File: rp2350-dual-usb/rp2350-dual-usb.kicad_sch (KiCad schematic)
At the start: 36 parts, among them J1 Conn_01x03_MountingPin, SW1 Button_Switch_SMD_Push_1P1T_W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, U1 LDL1117-3.3, U2 RP2354_60QFN, Y1 12MHz

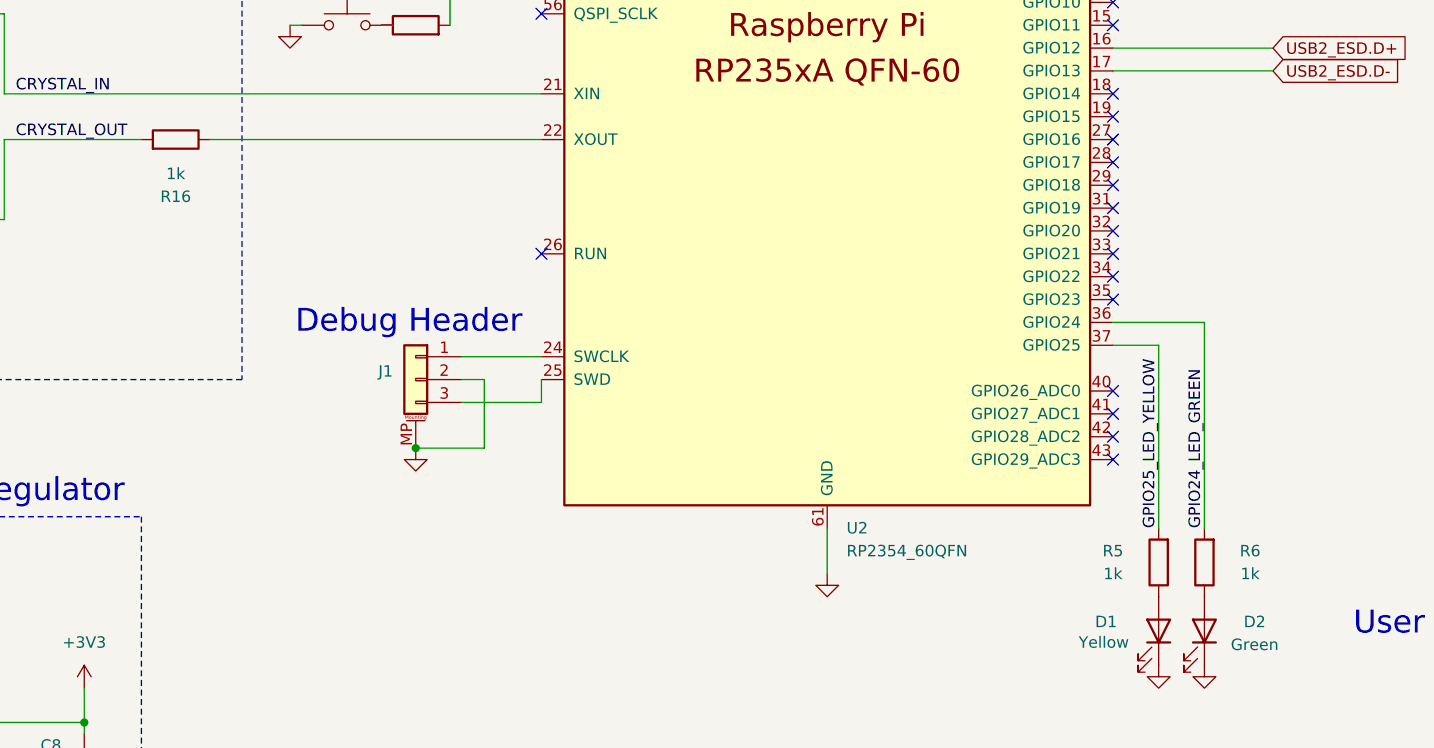
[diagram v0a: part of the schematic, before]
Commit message: Updates YouMe Transformer to v1.1, fixing incorrect R10 value. Improves the consistency of the Lichen symbol library.
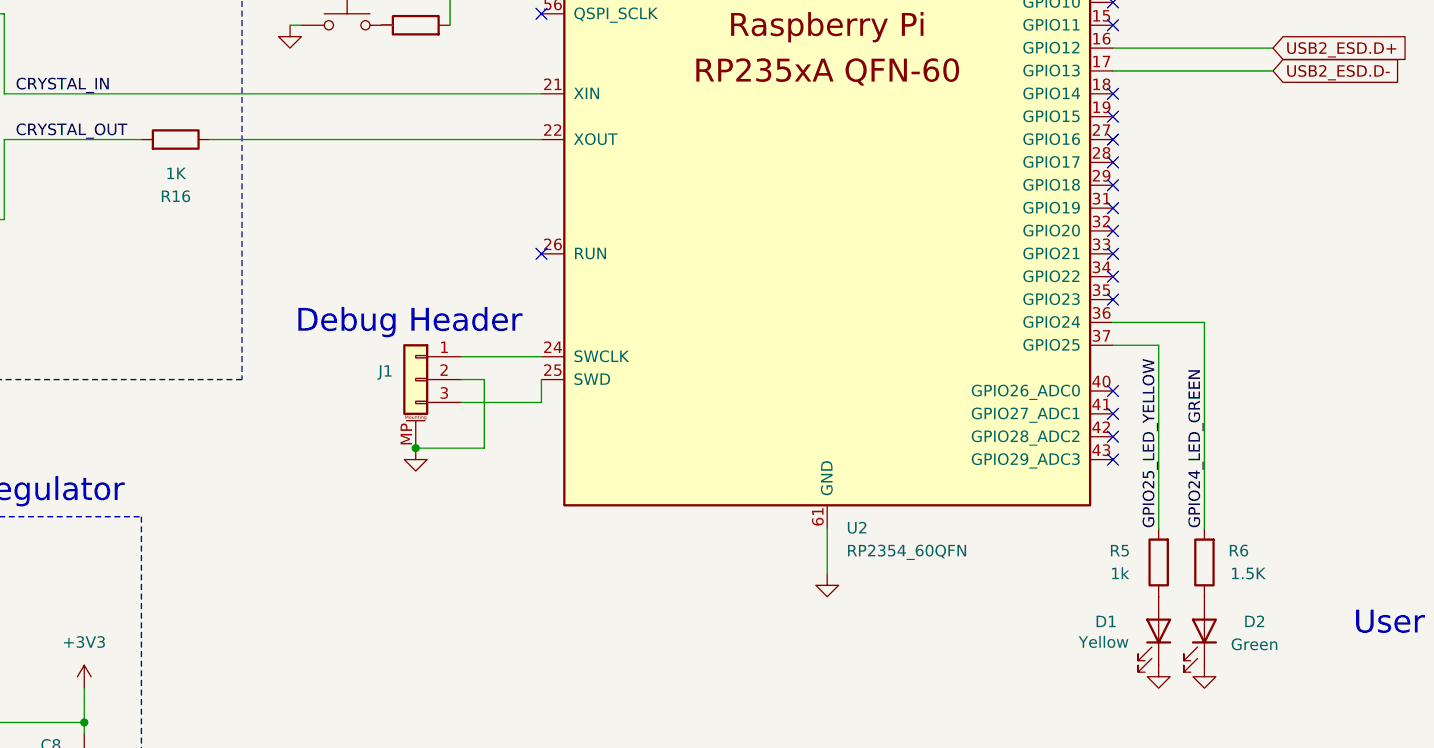
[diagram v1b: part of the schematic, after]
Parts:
- C1, C11, C6: value 100nF_0402_50V -> 100nF; Specifications 100nF 50V X7R ±10% 0402 -> (none)
- C10, C3, C7, C9: value 4.7uF_0402 -> 4.7uF; Specifications 10V 4.7uF X5R ±20% 0402 -> (none)
- C12, C13, C14, C15, C17, C18, C19: value 100nF_0402_16V -> 100nF; Specifications 100nF 50V X7R ±10% 0402 -> (none)
- C16: value 100nF_0603_16V -> 100nF; Specifications 100nF 50V X7R ±10% 0402 -> (none)
- C2: value 1uF_0805_50V -> 1uF; Specifications 1uF 50V X7R ±10% 0805 -> (none)
- C4, C5: value 15pF_0402 -> 15pF; Specifications 15pF 50V C0G ±5% 0402 MLCC -> (none)
- C8: value 4.7uF_0805_25V -> 4.7uF; Specifications 25V 4.7uF X5R ±10% 0805 -> (none)
- D1: symbol Lichen:LED_0805_JLC_Basic -> Lichen:LED_0805_JLC_Basic_Yellow; Part Number KT-0805Y -> KT-0805
- D2: symbol Lichen:LED_0805_JLC_Basic -> Lichen:LED_0805_JLC_Basic_Green; LCSC C2297 -> C2296; Part Number KT-0805G -> KT-0805
- J1: Manufacturer JST -> JST
- R16: value 1k_0402 -> 1K; Display 1k -> 1K
- R2: value 1k_0402 -> 1k
- R3: value 27R_0402 -> 27R
- R4: value 33R_0402 -> 27R
- R5: value 1k_0402 -> 1K
- R6: value 1k_0402 -> 1K; symbol Lichen:1k_0402 -> Lichen:1.5k_0402; Display 1k -> 1.5K; LCSC C11702 -> C25867; Part Number 0402WGF1001TCE -> 0402WGF1501TCE
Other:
- company: (none) -> Lichen Community Systems Worker Cooperative Canada
- title: (none) -> YouMe Transformer

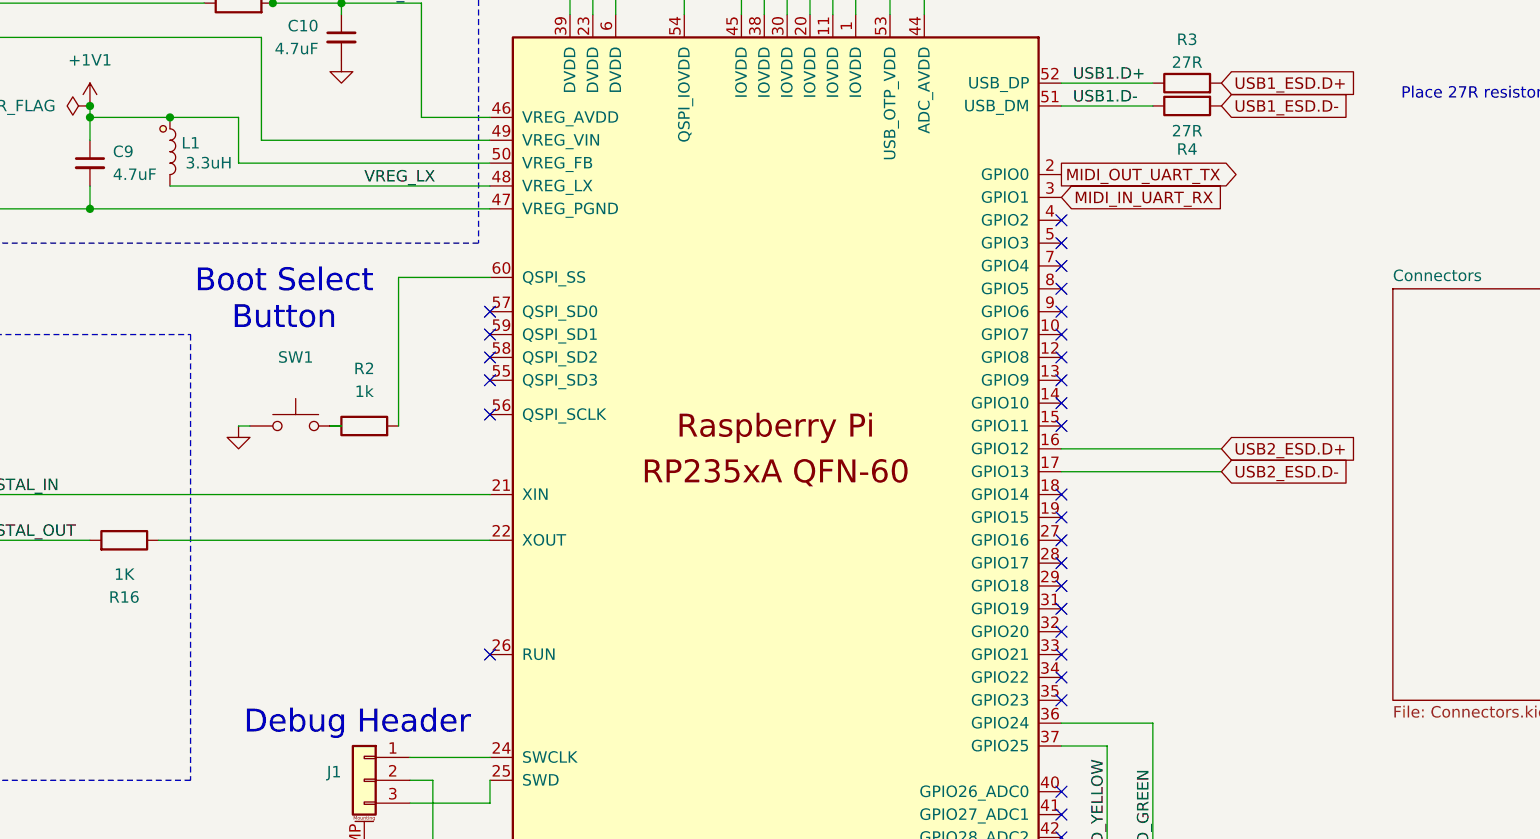
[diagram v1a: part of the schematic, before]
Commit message: feat: Updates symbol libraries and design blocks. Adds in-progress RP2350-based module.
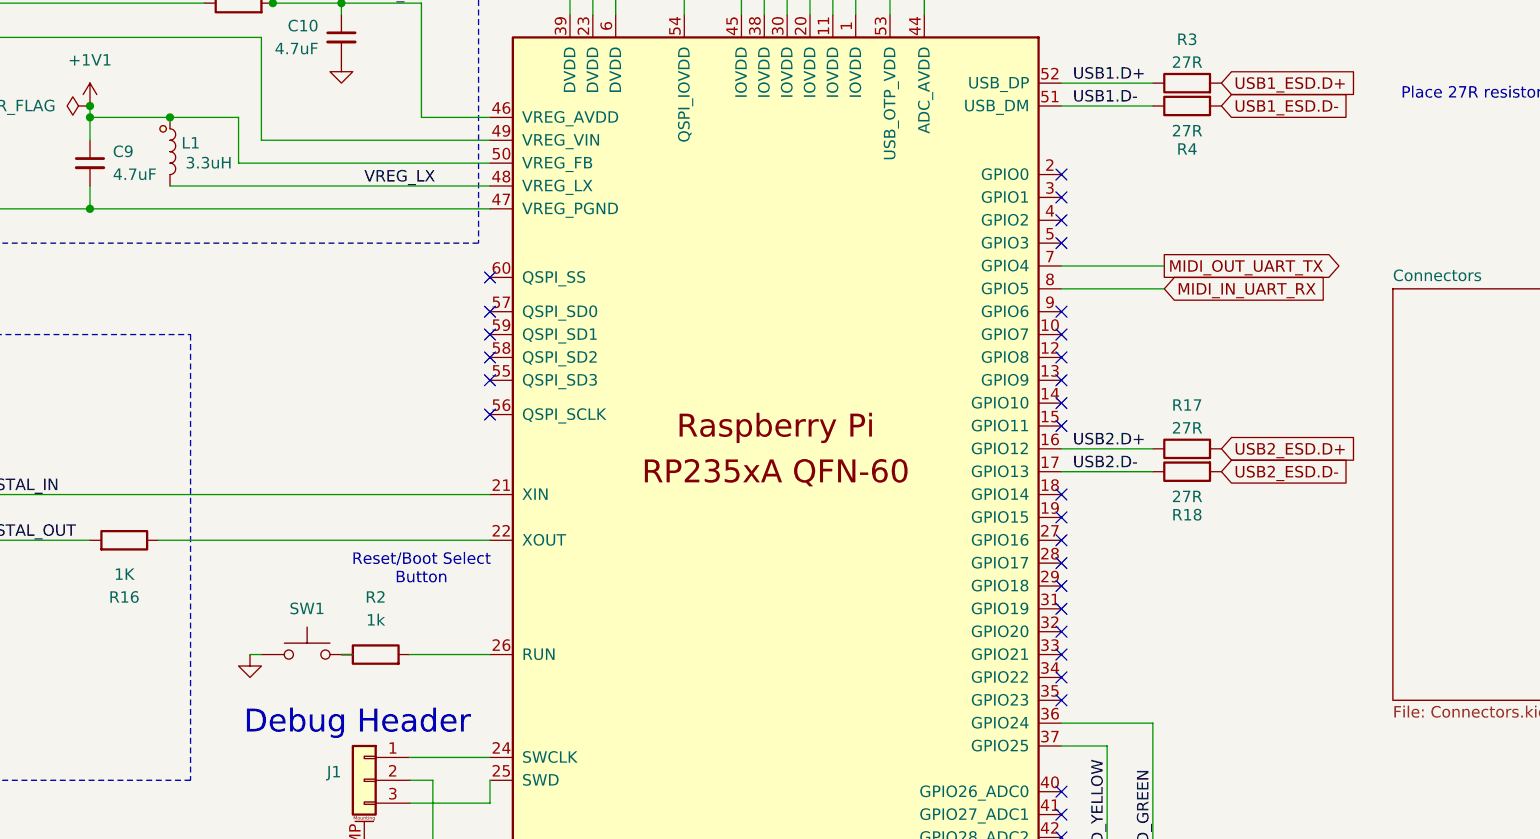
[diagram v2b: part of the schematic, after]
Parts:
- added R17, R18: 27R, Lichen:R_0402_1005Metric, symbol Lichen:27R_0402
- R6: value 1K -> 1.5K
- SW1: footprint Lichen:SW_Push_1P1T_NO_Vertical_Wuerth_434133025816 -> Button_Switch_SMD:SW_SPST_TS-1088-xR020; symbol Lichen:Button_Switch_SMD_Push_1P1T_Wurth -> Lichen:Button_Switch_SMD_Push_1P1T_XUNPU_Basic; LCSC C5504987 -> C720477; Manufacturer Wurth Elektronik -> XUNPU; Part Number 434133025816 -> TS-1088-AR02016
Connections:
- net MIDI_IN_UART_RX: now also U2.8 (GPIO5); no longer U2.3 (GPIO1)
- net MIDI_OUT_UART_TX: now also U2.7 (GPIO4); no longer U2.2 (GPIO0)
- net USB2_ESD.D+: now also R17.2; no longer U2.16 (GPIO12)
- net USB2_ESD.D-: now also R18.2; no longer U2.17 (GPIO13)
- net at U2.26 (RUN): now also R2.2
- net at U2.60 (QSPI_SS): no longer R2.2
- new net USB2.D+: R17.1, U2.16 (GPIO12)
- new net USB2.D-: R18.1, U2.17 (GPIO13)
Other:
- note added: "Reset/Boot Select Button"
- note removed: "Boot Select Button"
- moved on the sheet: R2, SW1

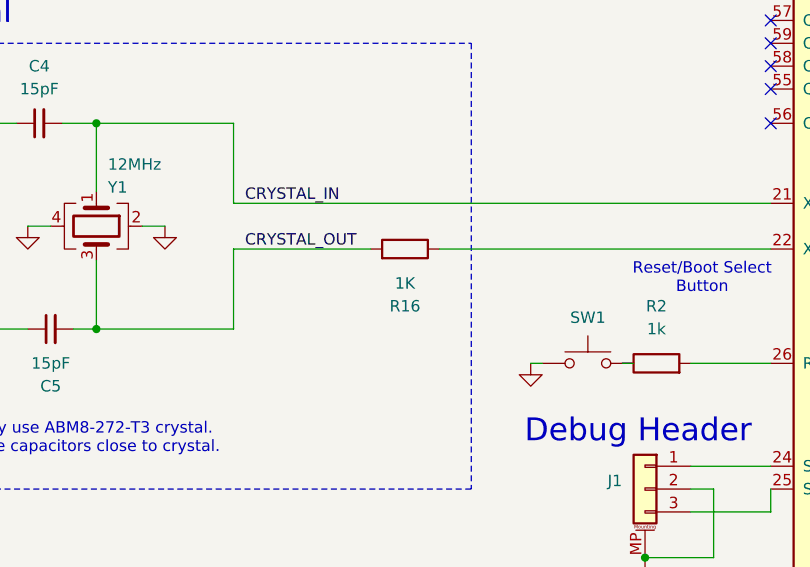
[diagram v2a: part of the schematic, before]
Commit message: feat: Updates Crustose, Cladonia and YouMe Transformer. Adds Stereo Latencies.
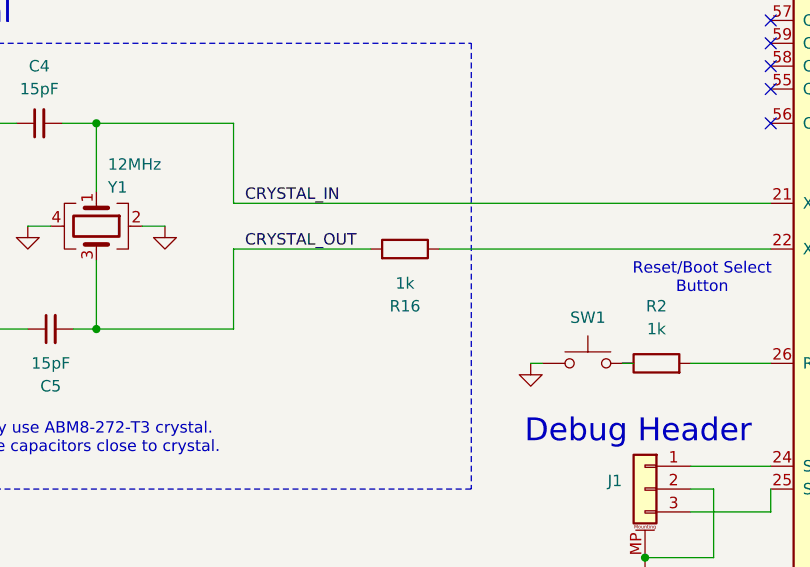
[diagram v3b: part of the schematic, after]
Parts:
- D1: footprint LED_SMD:LED_0805_2012Metric -> LED_SMD:LED_0805_2012Metric_Pad1.15x1.40mm_HandSolder; Part Number KT-0805 -> KT-0805Y
- D2: footprint LED_SMD:LED_0805_2012Metric -> LED_SMD:LED_0805_2012Metric_Pad1.15x1.40mm_HandSolder; LCSC C2296 -> C2297; Part Number KT-0805 -> KT-0805G
- J1: symbol Lichen:Raspberry_Pi_Pico_Debug_Header_JST -> Lichen:Raspberry_Pi_Pico_Debug_Header_JST_Horizontal
- R1: value 33R_0402 -> 33R
- R16: Display 1K -> 1k
- SW1: value Button_Switch_SMD_Push_1P1T_Wurth -> 1P1T Switch
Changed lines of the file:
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@@
 	)
 	(symbol
-		(lib_id "Lichen:Raspberry_Pi_Pico_Debug_Header_JST")
+		(lib_id "Lichen:Raspberry_Pi_Pico_Debug_Header_JST_Horizontal")
 		(at 101.6 128.27 0)
 		(mirror y)
@@
 		)
 		(instances
-			(project ""
+			(project "rp2350-dual-usb"
 				(path "/16ef7e10-64b2-4124-9408-fecb81ad1271"
 					(reference "J1")
@@
 		)
 		(instances
-			(project ""
+			(project "rp2350-dual-usb"
 				(path "/16ef7e10-64b2-4124-9408-fecb81ad1271"
 					(reference "R3")
@@
 		)
 		(instances
-			(project ""
+			(project "rp2350-dual-usb"
 				(path "/16ef7e10-64b2-4124-9408-fecb81ad1271"
 					(reference "C11")
@@
 			)
 		)
-		(property "Footprint" "LED_SMD:LED_0805_2012Metric"
+		(property "Footprint" "LED_SMD:LED_0805_2012Metric_Pad1.15x1.40mm_HandSolder"
 			(at 189.23 156.21 0)
 			(effects
@@
 			)
 		)
-		(property "Datasheet" "https://jlcpcb.com/api/file/downloadByFileSystemAccessId/8579709195039801344"
+		(property "Datasheet" "https://jlcpcb.com/api/file/downloadByFileSystemAccessId/8639582106239348736"
 			(at 189.23 156.21 0)
 			(effects
@@
 			)
 		)
-		(property "Description" "1.8V~2.4V 120° 175mcd 40mW 584nm~594nm 596nm Water Clear Yellow 0805"
+		(property "Description" "100mW 120° 2.6V~3.1V 430mcd 513nm~528nm 525nm 5mA Emerald Green Water Clear 0805"
 			(at 189.23 156.21 0)
 			(effects
@@
 			)
 		)
-		(property "Part Number" "KT-0805"
+		(property "Part Number" "KT-0805G"
 			(at 189.23 156.21 0)
 			(effects
@@
 			)
 		)
-		(property "LCSC" "C2296"
+		(property "LCSC" "C2297"
 			(at 189.23 156.21 0)
 			(effects
@@
 		)
 		(instances
-			(project ""
+			(project "rp2350-dual-usb"
 				(path "/16ef7e10-64b2-4124-9408-fecb81ad1271"
 					(reference "H1")
@@
 		)
 		(instances
-			(project ""
+			(project "rp2350-dual-usb"
 				(path "/16ef7e10-64b2-4124-9408-fecb81ad1271"
 					(reference "U2")
@@
 		)
 		(instances
-			(project ""
+			(project "rp2350-dual-usb"
 				(path "/16ef7e10-64b2-4124-9408-fecb81ad1271"
 					(reference "Y1")
@@
 		)
 		(instances
-			(project ""
+			(project "rp2350-dual-usb"
 				(path "/16ef7e10-64b2-4124-9408-fecb81ad1271"
 					(reference "#PWR013")
@@
 		)
 		(instances
-			(project ""
+			(project "rp2350-dual-usb"
 				(path "/16ef7e10-64b2-4124-9408-fecb81ad1271"
 					(reference "L1")
@@
 		)
 		(instances
-			(project ""
+			(project "rp2350-dual-usb"
 				(path "/16ef7e10-64b2-4124-9408-fecb81ad1271"
 					(reference "H2")
@@
 		)
 		(instances
-			(project ""
+			(project "rp2350-dual-usb"
 				(path "/16ef7e10-64b2-4124-9408-fecb81ad1271"
 					(reference "C5")
@@
 			)
 		)
-		(property "Display" "1K"
+		(property "Display" "1k"
 			(at 74.93 105.41 90)
 			(effects
@@
 		)
 		(instances
-			(project ""
+			(project "rp2350-dual-usb"
 				(path "/16ef7e10-64b2-4124-9408-fecb81ad1271"
 					(reference "R16")
@@
 		)
 		(instances
-			(project ""
+			(project "rp2350-dual-usb"
 				(path "/16ef7e10-64b2-4124-9408-fecb81ad1271"
 					(reference "R6")
@@
 			)
 		)
-		(property "Footprint" "LED_SMD:LED_0805_2012Metric"
+		(property "Footprint" "LED_SMD:LED_0805_2012Metric_Pad1.15x1.40mm_HandSolder"
 			(at 184.15 156.21 0)
 			(effects
@@
 			)
 		)
-		(property "Part Number" "KT-0805"
+		(property "Part Number" "KT-0805Y"
 			(at 184.15 156.21 0)
 			(effects
@@
 		)
 		(instances
-			(project ""
+			(project "rp2350-dual-usb"
 				(path "/16ef7e10-64b2-4124-9408-fecb81ad1271"
 					(reference "D1")
@@
 		)
 		(instances
-			(project ""
+			(project "rp2350-dual-usb"
 				(path "/16ef7e10-64b2-4124-9408-fecb81ad1271"
 					(reference "R2")
@@
 			)
 		)
-		(property "Value" "Button_Switch_SMD_Push_1P1T_Wurth"
+		(property "Value" "1P1T Switch"
 			(at 95.25 109.22 0)
 			(effects
@@
 		)
 		(instances
-			(project ""
+			(project "rp2350-dual-usb"
 				(path "/16ef7e10-64b2-4124-9408-fecb81ad1271"
 					(reference "SW1")
@@
 			)
 		)
-		(property "Value" "33R_0402"
+		(property "Value" "33R"
 			(at 87.63 44.45 90)
 			(effects
@@
 		)
 		(instances
-			(project ""
+			(project "rp2350-dual-usb"
 				(path "/16ef7e10-64b2-4124-9408-fecb81ad1271"
 					(reference "R1")
@@
 		)
 		(instances
-			(project ""
+			(project "rp2350-dual-usb"
 				(path "/16ef7e10-64b2-4124-9408-fecb81ad1271"
 					(reference "C9")
@@
 		)
 		(instances
-			(project ""
+			(project "rp2350-dual-usb"
 				(path "/16ef7e10-64b2-4124-9408-fecb81ad1271"
 					(reference "#PWR010")
@@
 		)
 		(instances
-			(project ""
+			(project "rp2350-dual-usb"
 				(path "/16ef7e10-64b2-4124-9408-fecb81ad1271"
 					(reference "#FLG01")
@@
 		)
 		(instances
-			(project ""
+			(project "rp2350-dual-usb"
 				(path "/16ef7e10-64b2-4124-9408-fecb81ad1271"
 					(reference "#PWR011")
